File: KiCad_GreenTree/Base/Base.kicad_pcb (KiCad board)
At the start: 2 copper layers, 22 parts, among them Q1 BCX56, Q2 BCX56, Q3 BCX56, Q4 BCX56, SW1 SW_DPDT_x2, U1 NE555D, U2 NE555D, U3 74HC04

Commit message: update
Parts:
- moved Q1 1.78 mm to (156.9, 105.1)
- moved Q4 1.02 mm to (156.9, 86.1)
- moved Q2 0.76 mm to (156.9, 98.8)
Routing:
- net VCC: track 166.5 -> 177.0 mm
- net /LED_MATRIX_2: track 31.7 -> 33.5 mm
- net Net-(Q1-Pad1): track 33.7 -> 35.3 mm
- net /LED_MATRIX_1: track 47.9 -> 46.3 mm
- net Net-(Q2-Pad1): track 32.0 -> 32.6 mm
- added copper zone on B.Cu, net VCC
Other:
- board outline added: 65 x 62.2 mm
- board text added: "Designed by Kai and Tobi in Karlsruhe"
- board text added: "Frohe Weihnachten"

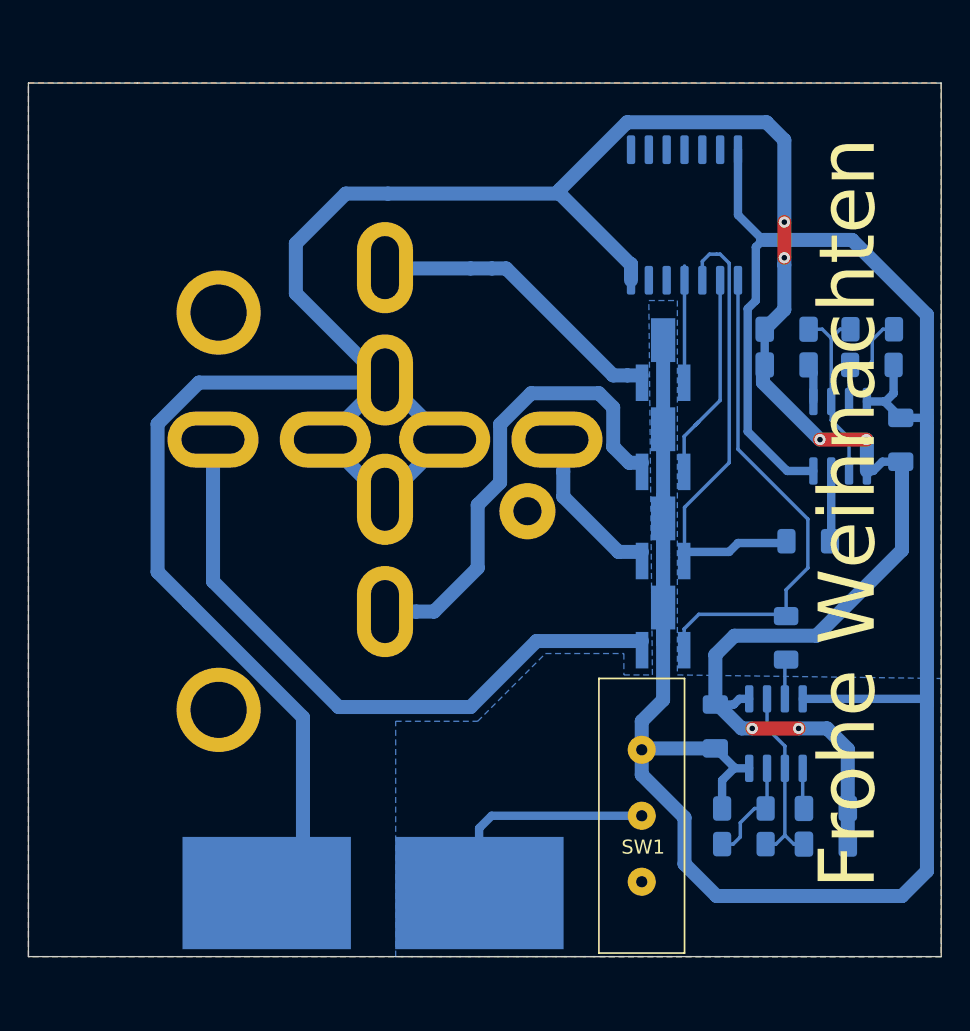
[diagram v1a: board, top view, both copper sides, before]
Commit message: ordentlicher Schaltplan
NO DRC errors anymore
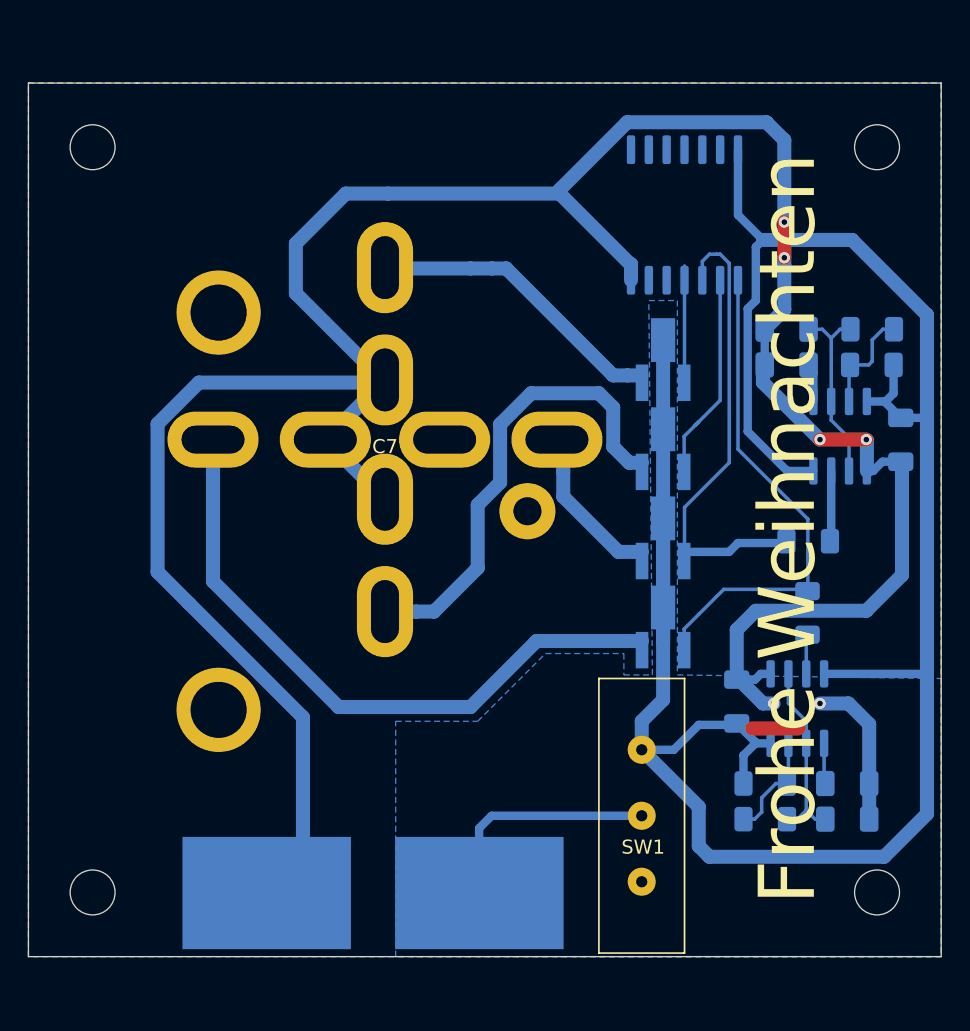
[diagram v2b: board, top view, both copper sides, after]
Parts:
- removed REF**: Verbindung_Basis, Bib:Verbindung_Basis
- added C7: Baum_Connector, Bib:Verbindung_Basis, F.Cu at (137.1, 92.4)
- added H1: M3, MountingHole:MountingHole_3.2mm_M3, F.Cu at (172.2, 71.6)
- added H2: M3, MountingHole:MountingHole_3.2mm_M3, F.Cu at (172.2, 124.7)
- added H3: M3, MountingHole:MountingHole_3.2mm_M3, F.Cu at (116.3, 71.6)
- added H4: M3, MountingHole:MountingHole_3.2mm_M3, F.Cu at (116.3, 124.7)
- moved C1 2.34 mm to (170.1, 116.9)
- moved C6 2.34 mm to (162.2, 111.1)
- moved R1 2.34 mm to (164.2, 116.9)
- moved R6 2.34 mm to (167.2, 104.8)
- moved C3 2.34 mm to (170.1, 119.5)
- moved R2 2.34 mm to (164.2, 119.5)
- moved U1 2.34 mm to (166.5, 111.6)
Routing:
- net GND: track 217.7 -> 204.5 mm
- net VCC: track 177.0 -> 171.7 mm

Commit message: Added Diodes
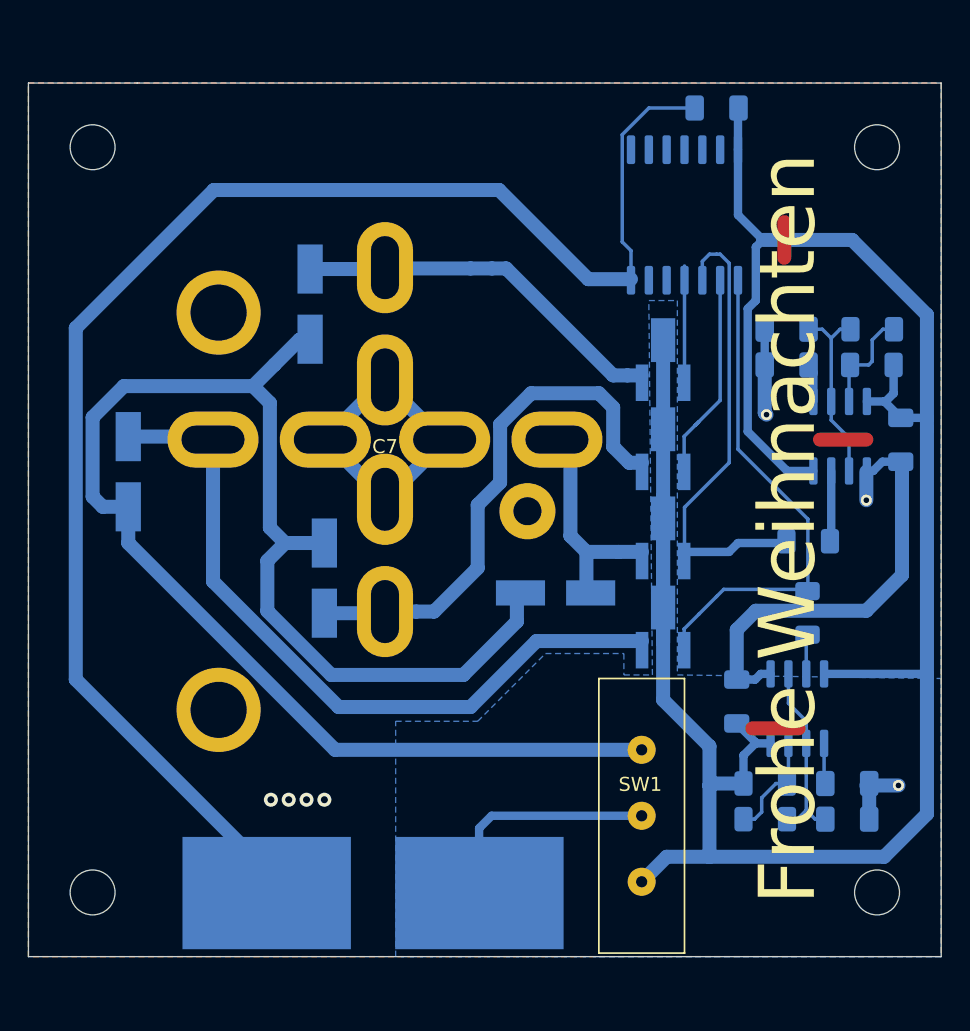
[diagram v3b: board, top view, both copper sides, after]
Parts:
- added C8: 100n, Capacitor_SMD:C_1206_3216Metric_Pad1.33x1.80mm_HandSolder, B.Cu at (160.7, 68.8)
- added D1: STPS 1L30A STM, Diode_SMD:D_SMA_Handsoldering, B.Cu at (131.8, 82.8)
- added D2: STPS 1L30A STM, Diode_SMD:D_SMA_Handsoldering, B.Cu at (149.3, 103.3)
- added D3: STPS 1L30A STM, Diode_SMD:D_SMA_Handsoldering, B.Cu at (132.8, 102.3)
- added D4: STPS 1L30A STM, Diode_SMD:D_SMA_Handsoldering, B.Cu at (118.8, 94.7)
- moved SW1 20.5 mm to (158.5, 109.4), turned to 270 degrees
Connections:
- SW1 pad 3: Net-(SW1-Pad3) -> +9V
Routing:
- net +9V: track 0.00 -> 115.1 mm
- net GND: track 204.5 -> 189.4 mm, vias 6 -> 7
- net /LED_MATRIX_4: track 21.4 -> 27.8 mm
- net /LED_MATRIX_1: track 46.3 -> 52.5 mm
- net /LED_MATRIX_2: track 33.5 -> 38.0 mm
- net /LED_MATRIX_3: track 11.6 -> 16.0 mm
- net VCC: track 171.7 -> 173.8 mm

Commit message: fixed Diodes
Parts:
- moved D2 32.5 mm to (116.8, 101.8), turned to 270 degrees
- moved D3 19.1 mm to (116.8, 91.9), turned to 270 degrees
- moved D4 17.9 mm to (116.8, 112.5)
- moved D1 15.0 mm to (116.8, 82.5)
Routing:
- net /LED_MATRIX_3: track 16.0 -> 74.3 mm
- net +9V: track 115.1 -> 77.5 mm
- net /LED_MATRIX_2: track 38.0 -> 68.5 mm
- net GND: track 189.4 -> 218.5 mm
- net /LED_MATRIX_4: track 27.8 -> 44.5 mm
- net /LED_MATRIX_1: track 52.5 -> 59.0 mm

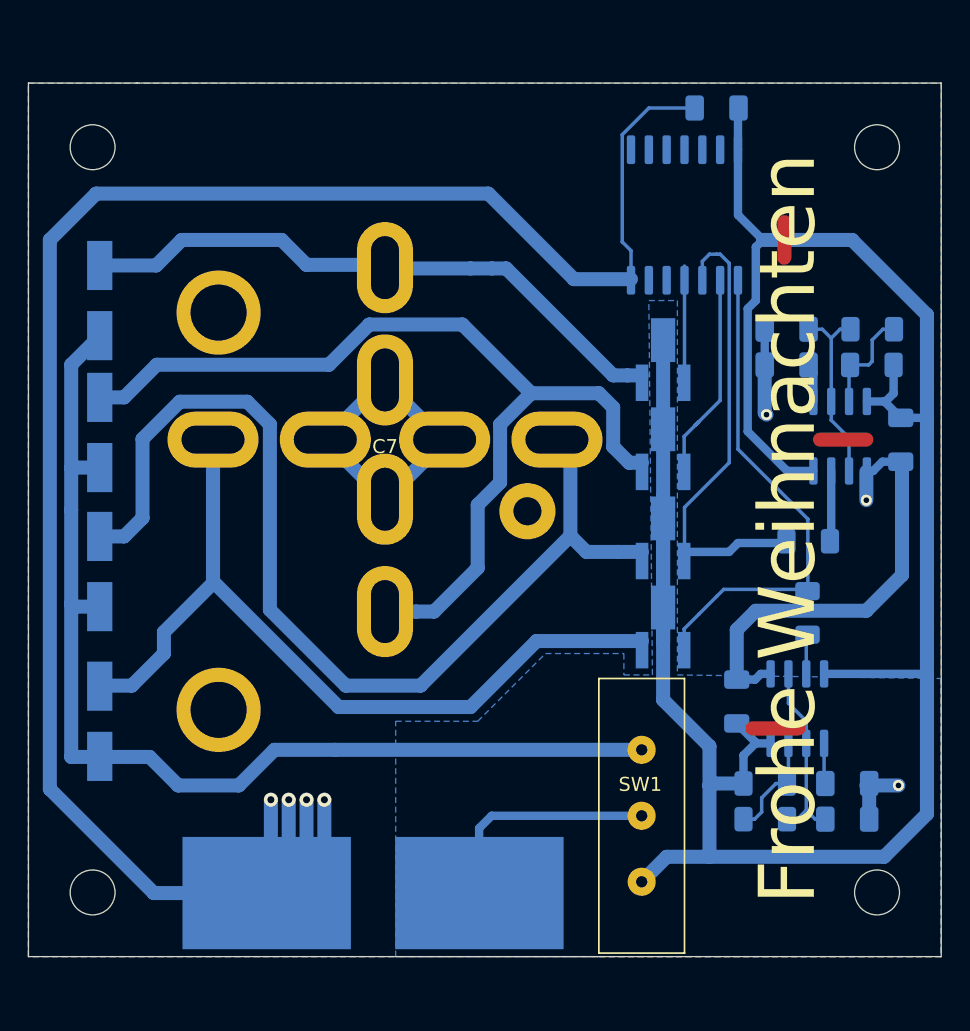
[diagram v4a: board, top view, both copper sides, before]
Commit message: added 5V
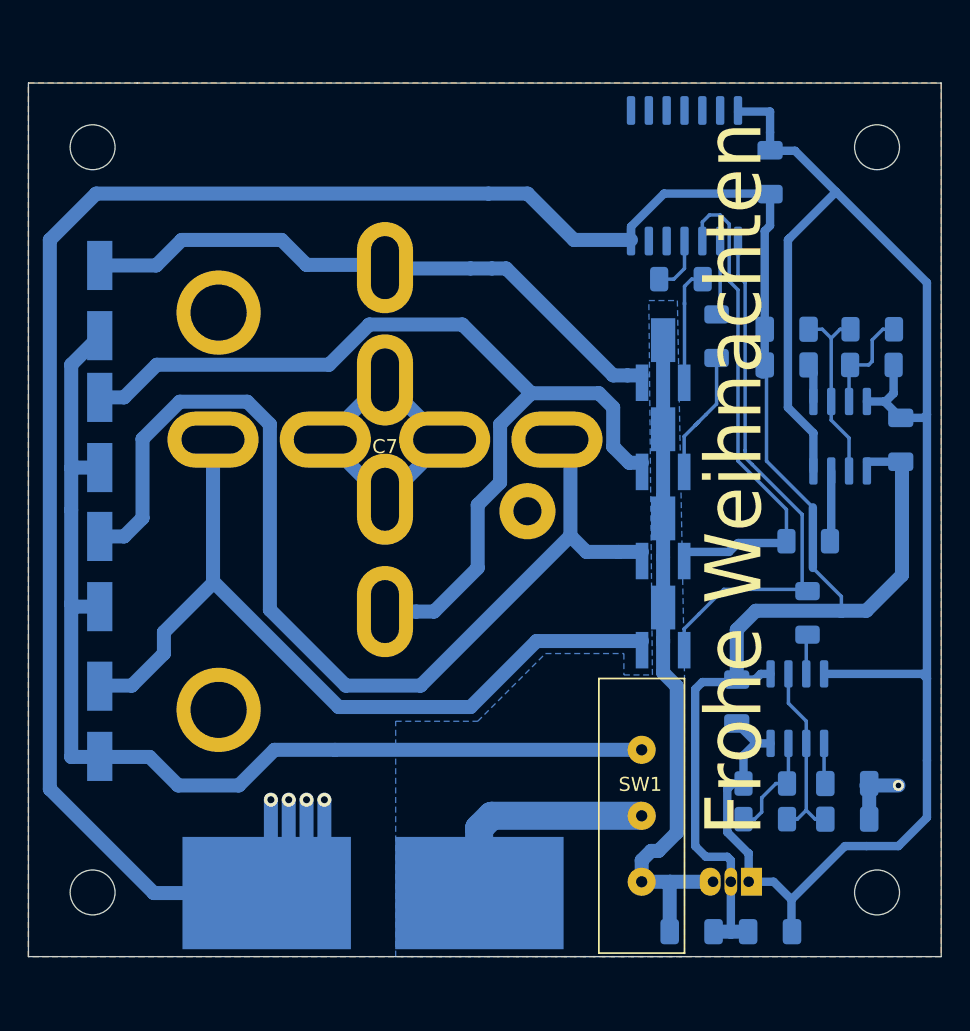
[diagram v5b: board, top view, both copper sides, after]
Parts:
- added C10: 10n, Capacitor_SMD:C_1206_3216Metric_Pad1.33x1.80mm_HandSolder, B.Cu at (164.6, 127.5)
- added C9: 330n, Capacitor_SMD:C_1206_3216Metric_Pad1.33x1.80mm_HandSolder, B.Cu at (159.0, 127.5)
- added R7: R, Resistor_SMD:R_1206_3216Metric_Pad1.30x1.75mm_HandSolder, B.Cu at (158.2, 81.0)
- added R8: R, Resistor_SMD:R_1206_3216Metric_Pad1.30x1.75mm_HandSolder, B.Cu at (160.7, 85.1)
- added U4: L78L05_TO92, Package_TO_SOT_THT:TO-92_Inline, B.Cu at (163.0, 123.9)
- moved C8 5.95 mm to (164.6, 73.4), turned to 270 degrees
- moved U3 2.79 mm to (158.5, 73.6)
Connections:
- C5 pad 1: VCC -> +5V
- C6 pad 1: VCC -> +5V
- C8 pad 1: VCC -> +5V
- R1 pad 1: VCC -> +5V
- R3 pad 1: VCC -> +5V
- U1 pad 4: VCC -> +5V
- U1 pad 8: VCC -> +5V
- U2 pad 4: VCC -> +5V
- U2 pad 8: VCC -> +5V
- U3 pad 14: VCC -> +5V
- U3 pad 2: Net-(Q3-Pad1) -> Net-(R8-Pad2)
- U3 pad 4: Net-(Q4-Pad1) -> Net-(R7-Pad2)
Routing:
- net +5V: track 0.00 -> 129.1 mm
- net VCC: track 173.8 -> 48.7 mm
- net GND: track 218.5 -> 252.7 mm, vias 7 -> 5
- net Net-(Q3-Pad1): track 14.4 -> 8.78 mm
- net Net-(R8-Pad2): track 0.00 -> 5.36 mm
- net Net-(R7-Pad2): track 0.00 -> 4.15 mm
- net Net-(Q2-Pad1): track 32.6 -> 35.7 mm
- net Net-(Q1-Pad1): track 35.4 -> 38.4 mm
- net Net-(Q4-Pad1): track 7.80 -> 8.73 mm

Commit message: fixed Inv
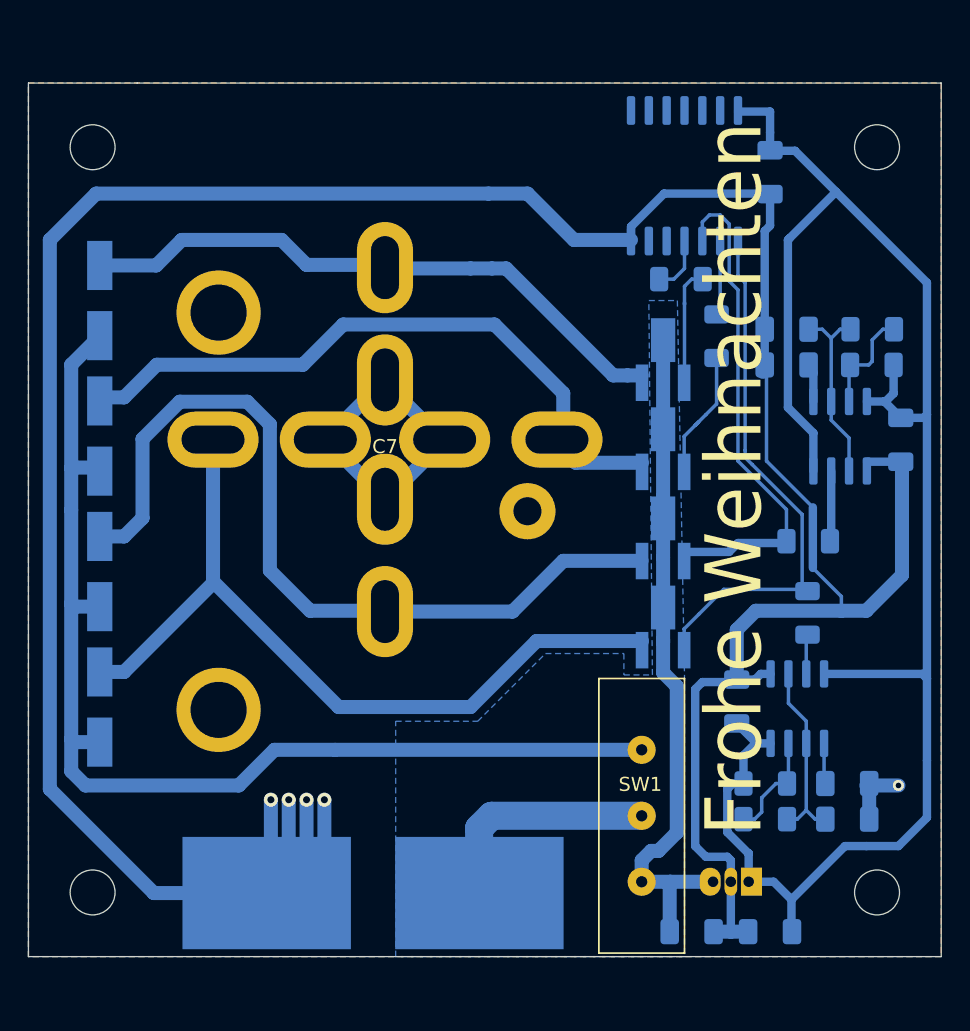
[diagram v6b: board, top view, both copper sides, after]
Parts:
- moved D3 9.91 mm to (116.8, 101.8)
- moved D2 9.65 mm to (116.8, 92.2)
- moved D4 1.02 mm to (116.8, 111.5)
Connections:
- Q2 pad 3: /LED_MATRIX_3 -> /LED_MATRIX_2
- Q3 pad 3: /LED_MATRIX_2 -> /LED_MATRIX_3
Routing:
- net /LED_MATRIX_3: track 74.3 -> 49.1 mm
- net /LED_MATRIX_2: track 68.5 -> 59.8 mm
- net +9V: track 77.5 -> 80.2 mm
- net /LED_MATRIX_1: track 59.0 -> 57.4 mm

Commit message: final
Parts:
- added G***: LOGO, grafics:star_silk, F.Cu at (171.8, 117.1)
- added G***: LOGO, grafics:frohe_weihnachten_dick, F.Cu at (166.0, 97.8)
- added G***: LOGO, grafics:star_silk, F.Cu at (160.0, 85.7)
- added G***: LOGO, grafics:star_silk, F.Cu at (171.8, 79.9)
- added G***: LOGO, grafics:star_silk, F.Cu at (160.3, 97.0)
- added G***: LOGO, grafics:star_silk, F.Cu at (160.9, 110.7)
- added G***: LOGO, grafics:star_silk, F.Cu at (171.8, 93.2)
- added G***: LOGO, grafics:star_silk, F.Cu at (162.5, 75.0)
- added G***: LOGO, grafics:star_silk, F.Cu at (171.7, 105.6)
- added G***: LOGO, grafics:star_silk, F.Cu at (163.0, 120.4)
- BT3: footprint Bib:9V_Holder -> Bib:9V ohne Loecher
- C1, C10, C2, C3, C4, C5, C6, C8, C9: footprint Capacitor_SMD:C_1206_3216Metric_Pad1.33x1.80mm_HandSolder -> Capacitor_SMD:C_0805_2012Metric_Pad1.18x1.45mm_HandSolder
- R1, R3: value R -> 10k; footprint Resistor_SMD:R_1206_3216Metric_Pad1.30x1.75mm_HandSolder -> Resistor_SMD:R_0805_2012Metric_Pad1.20x1.40mm_HandSolder
- R2, R4: footprint Resistor_SMD:R_1206_3216Metric_Pad1.30x1.75mm_HandSolder -> Resistor_SMD:R_0805_2012Metric_Pad1.20x1.40mm_HandSolder
- R5, R6: value R -> 1k
- R7, R8: value R -> 1k; footprint Resistor_SMD:R_1206_3216Metric_Pad1.30x1.75mm_HandSolder -> Resistor_SMD:R_0805_2012Metric_Pad1.20x1.40mm_HandSolder
- moved C1 4.14 mm to (170.6, 112.8), turned to 90 degrees
- moved C2 3.86 mm to (165.4, 90.9), turned to 270 degrees
- moved C3 1.47 mm to (170.6, 118.1)
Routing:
- net +5V: track 129.1 -> 147.6 mm
- net +9V: track 80.2 -> 85.1 mm
- net GND: track 252.7 -> 248.7 mm
- net Net-(Q4-Pad1): track 8.73 -> 7.03 mm
- net Net-(C1-Pad1): track 2.90 -> 2.21 mm
- net Net-(R8-Pad2): track 5.36 -> 5.92 mm
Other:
- board text added: "Designed by Tobi and Kai in Karlsruhe"
- board text removed: "Designed by Kai and Tobi in Karlsruhe"
- board text removed: "Frohe Weihnachten"
